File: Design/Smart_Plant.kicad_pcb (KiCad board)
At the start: 2 copper layers, 80 x 129.1 mm, 75 parts, among them IC1 TP4056, IC2 TLC555CDR, IC3 AHT20, IC4 RT9080-33GJ5, IC5 ESP32-S2-MINI-1-N4R2, IC6 VEML7700-TR, IC7 MAX17048G+T10, J6 USB-C, Q1 IRLML0100, T1 MMBT2222A, T2 LBSS84LT1G

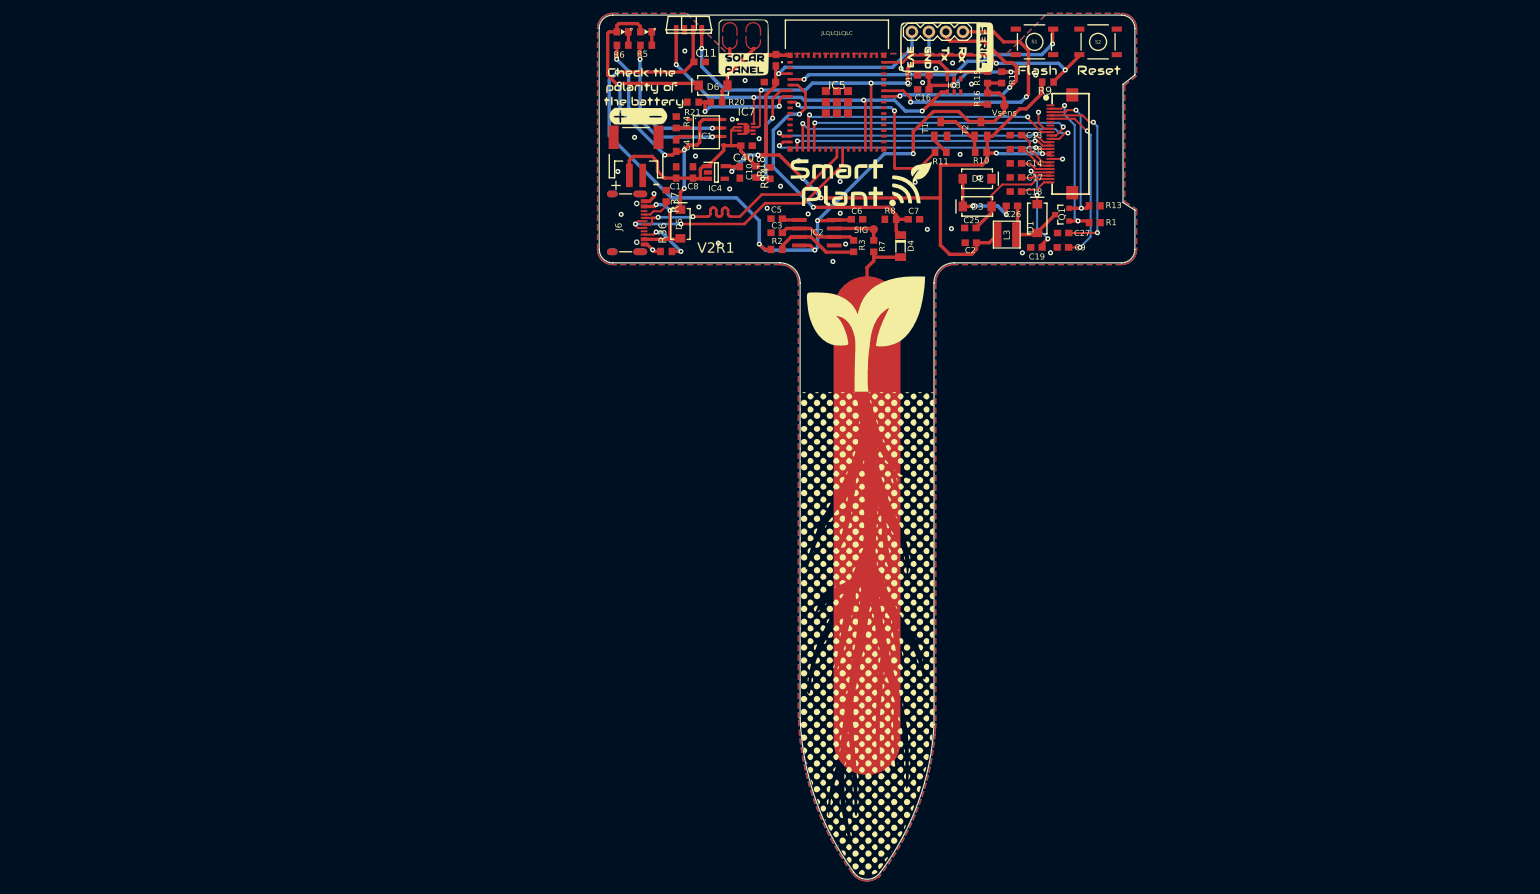
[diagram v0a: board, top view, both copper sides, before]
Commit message: V2R2 (XL): larger Smart Plant board variant
KiCad schematic/PCB/project updated for the XL version, GND fix,
fabrication toolkit options and production outputs (BOM, positions,
netlist, gerber zip), plus refreshed silkscreen documentation.

Co-Authored-By: Claude Opus 5.5 <noreply@anthropic.com>
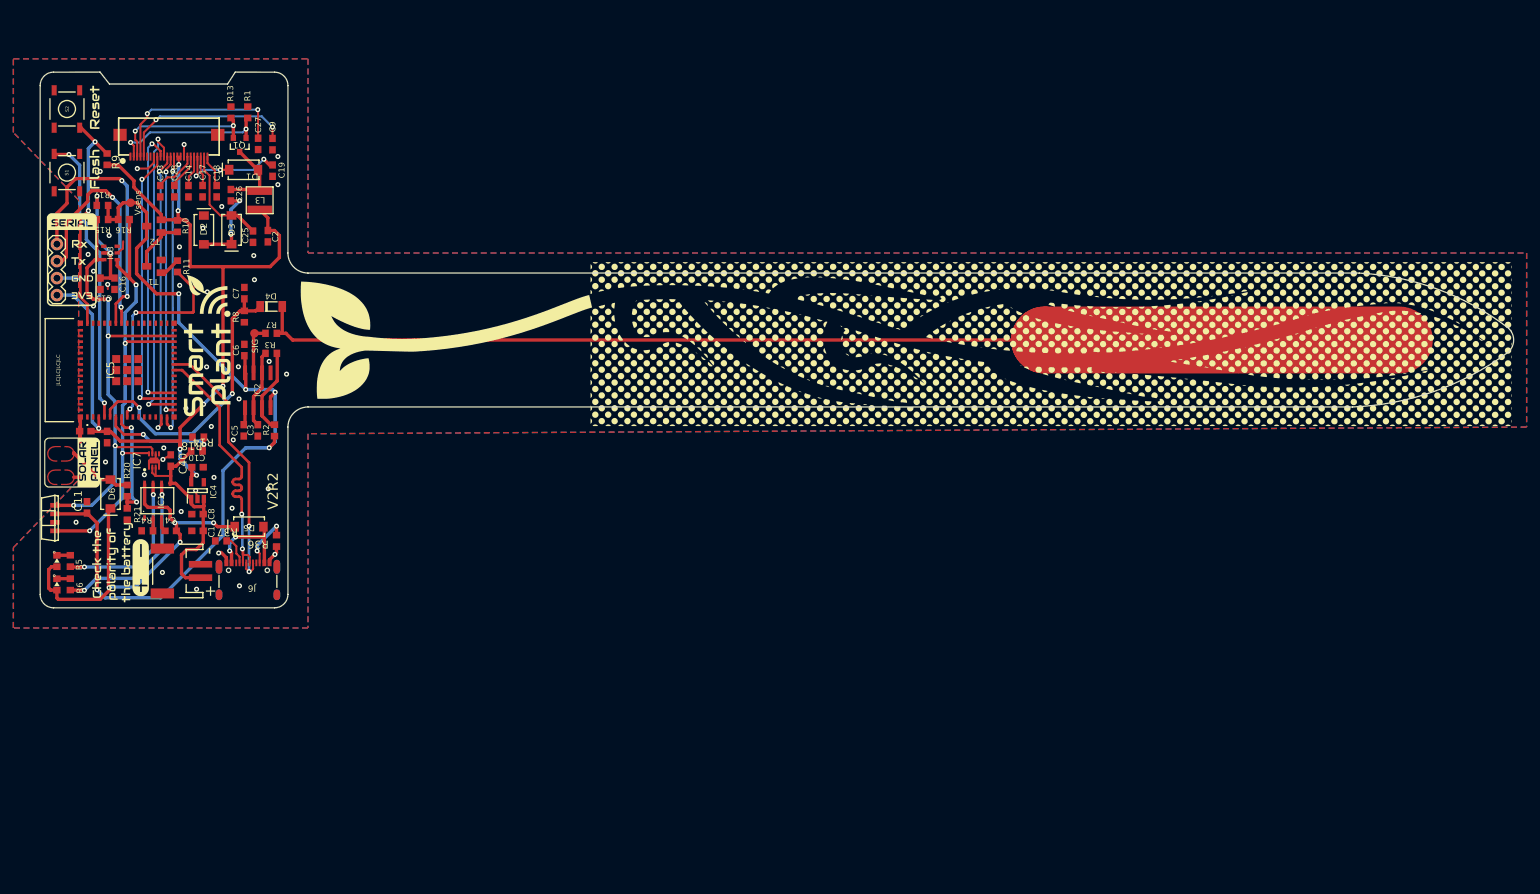
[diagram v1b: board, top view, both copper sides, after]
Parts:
- removed G*** (x2): LOGO, LOGO
- added ?: LOGO, LOGO, F.Cu at (135.0, 89.6)
- added ?: LOGO, LOGO, B.Cu at (135.0, 89.6)
- moved S2 154.3 mm to (29.0, 54.5), turned to 90 degrees
- moved S1 145.8 mm to (29.0, 64.0), turned to -90 degrees
- moved R9 141.0 mm to (35.0, 62.0), turned to -90 degrees
- moved R17 135.7 mm to (34.3, 68.9), turned to 180 degrees
- moved FPC 134.9 mm to (44.2, 58.4), turned to 180 degrees
- moved R15 133.9 mm to (34.3, 71.0), turned to 180 degrees
- moved J5 133.6 mm to (27.5, 82.3), turned to 90 degrees
- moved TP2 131.3 mm to (38.5, 68.5), turned to 180 degrees
- moved R16 130.2 mm to (37.5, 71.0), turned to 0 degrees
- moved R13 129.8 mm to (53.5, 55.0), turned to 90 degrees
- moved IC3 128.5 mm to (35.5, 76.0), turned to 0 degrees
- moved C13 128.1 mm to (42.9, 66.8), turned to 90 degrees
- moved R1 127.6 mm to (56.0, 55.0), turned to 90 degrees
- moved C15 126.8 mm to (34.0, 80.6), turned to -90 degrees
- moved C28 125.8 mm to (45.0, 66.8), turned to 90 degrees
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- renumbered FPC0 to FPC
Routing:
- net PROBE: track 77.6 -> 172.1 mm
- net GND: track 26.9 -> 32.4 mm, vias 37 -> 41
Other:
- board size 80 x 129.1 mm -> 220.1 x 80 mm
- board text added: "V2R2"
- board text removed: "V2R1"
